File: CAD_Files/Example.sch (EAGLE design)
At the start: 9 parts, among them IC1 LM555D, Q1 BSS806N

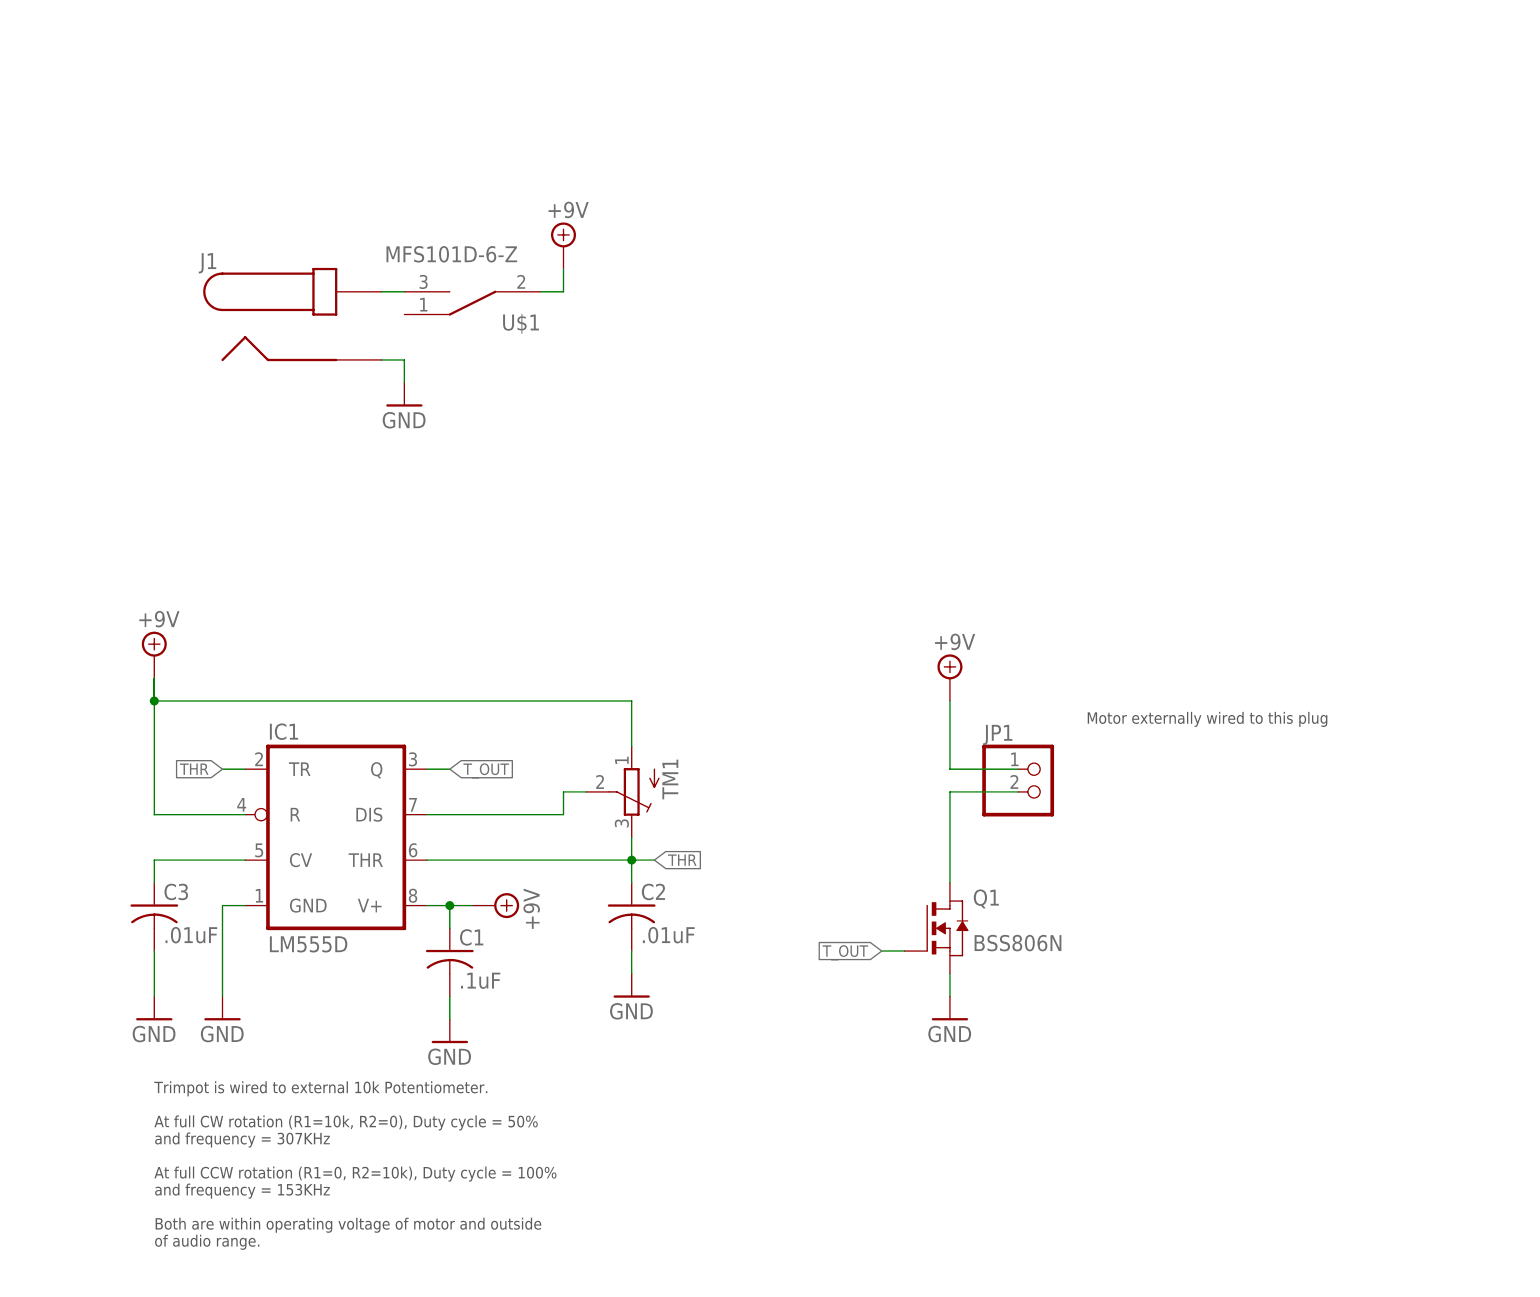
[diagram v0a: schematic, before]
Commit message: Added decoupling capacitors, fixed Library style guide compliance
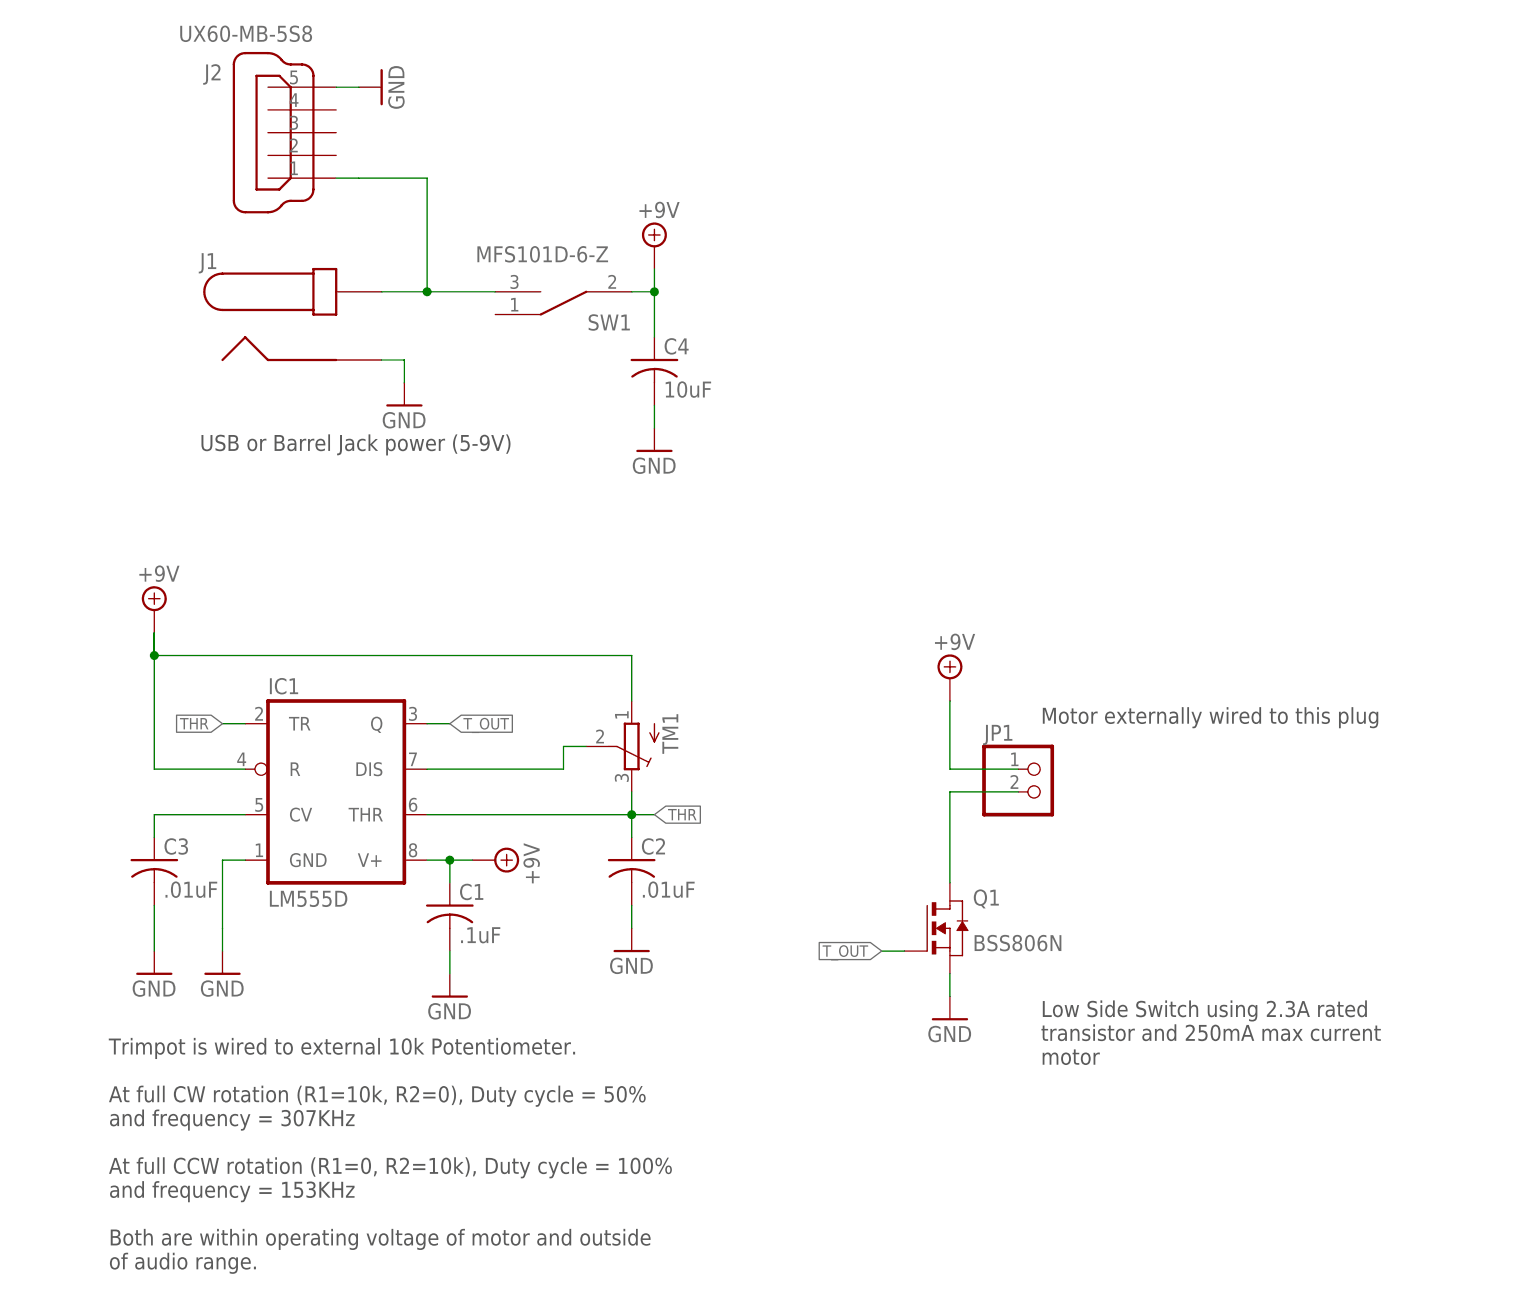
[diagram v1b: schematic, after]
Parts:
- removed U$1: MFS101D-6-Z, Example:MFS101D-6-Z
- added C4: 10uF, rcl:C-USC0603
- added J2: UX60-MB-5S8, RoboJackets-Connectors:UX60-MB-5S8
- added SW1: MFS101D-6-Z, Example:MFS101D-6-Z
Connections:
- removed net N$4: J1.1, U$1.B
- new net N$5: J1.1, J2.1, SW1.B
- net +9V: now also C4.1, SW1.COMMON; no longer U$1.COMMON
- net GND: now also C4.2, J2.5
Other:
- note added: "Low Side Switch using 2.3A rated transistor and 250mA max current motor"
- note added: "USB or Barrel Jack power (5-9V)"
- moved on the sheet: C1, C2, C3, IC1, TM1

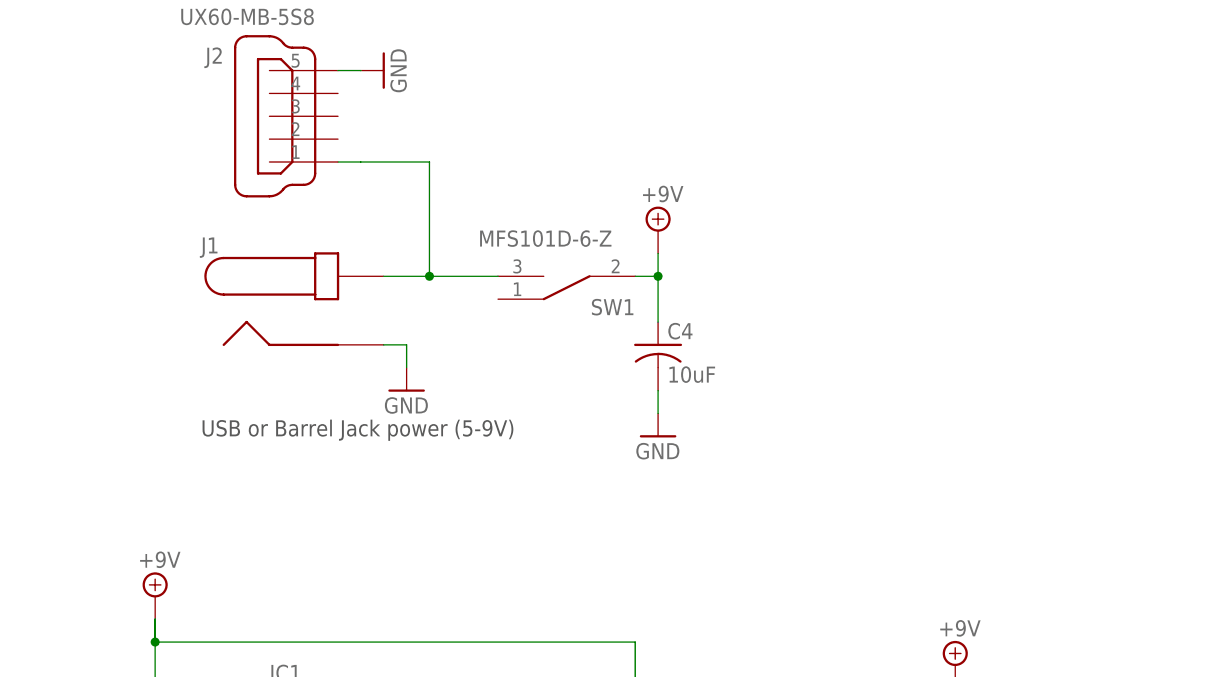
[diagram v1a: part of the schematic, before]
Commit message: Library edits, power switching transistor, 3d CAD
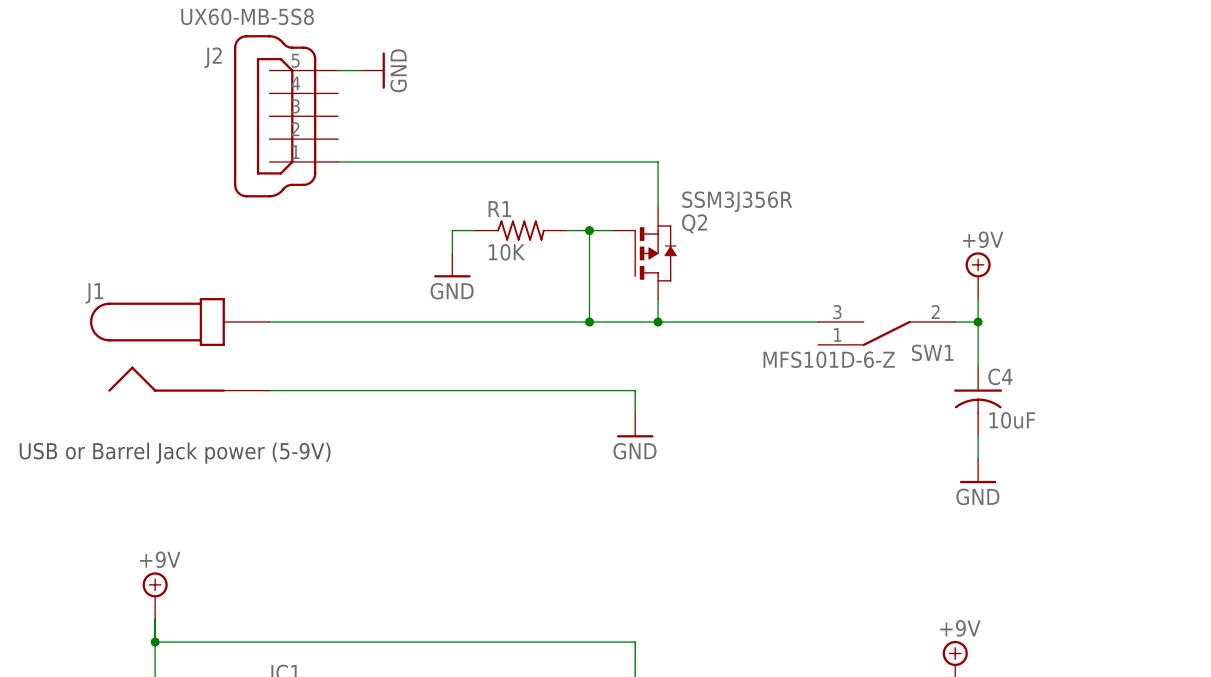
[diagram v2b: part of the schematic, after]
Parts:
- added Q2: SSM3J356R, Example:SSM3J356R
- added R1: 10K, rcl:R-US_R0603
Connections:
- removed net N$5: J1.1, J2.1, SW1.B
- new net N$4: J2.1, Q2.S
- new net N$6: J1.1, Q2.D, Q2.G, R1.2, SW1.B
- net GND: now also R1.1
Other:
- moved on the sheet: C4, J1, SW1
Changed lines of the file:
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@@
 <?xml version="1.0" encoding="utf-8"?>
 <!DOCTYPE eagle SYSTEM "eagle.dtd">
-<eagle version="9.5.2">
+<eagle version="9.6.2">
 <drawing>
 <settings>
@@
 <part name="SUPPLY12" library="RoboJackets-Supplies" deviceset="GND" device=""/>
 <part name="SW1" library="Example" deviceset="MFS101D-6-Z" device=""/>
+<part name="SUPPLY13" library="RoboJackets-Supplies" deviceset="GND" device=""/>
+<part name="R1" library="rcl" library_urn="urn:adsk.eagle:library:334" deviceset="R-US_" device="R0603" package3d_urn="urn:adsk.eagle:package:23555/3" value="10K"/>
+<part name="Q2" library="Example" deviceset="SSM3J356R" device="" package3d_urn="urn:adsk.eagle:package:24993154/1"/>
 </parts>
 <sheets>
@@
 transistor and 250mA max current
 motor</text>
-<text x="33.02" y="99.06" size="1.778" layer="97">USB or Barrel Jack power (5-9V)</text>
+<text x="12.7" y="96.52" size="1.778" layer="97">USB or Barrel Jack power (5-9V)</text>
 </plain>
 <instances>
@@
 <attribute name="VALUE" x="114.3" y="33.02" size="1.778" layer="96"/>
 </instance>
-<instance part="J1" gate="G$1" x="43.18" y="111.76" smashed="yes">
-<attribute name="NAME" x="33.02" y="119.38" size="1.778" layer="95"/>
-<attribute name="VALUE" x="33.02" y="106.68" size="1.778" layer="96"/>
+<instance part="J1" gate="G$1" x="30.48" y="106.68" smashed="yes">
+<attribute name="NAME" x="20.32" y="114.3" size="1.778" layer="95"/>
+<attribute name="VALUE" x="20.32" y="101.6" size="1.778" layer="96"/>
 </instance>
 <instance part="JP1" gate="G$1" x="127" y="60.96" smashed="yes">
@@
 <attribute name="VALUE" x="114.935" y="76.835" size="1.778" layer="96"/>
 </instance>
-<instance part="SUPPLY8" gate="G$1" x="55.88" y="104.14" smashed="yes">
-<attribute name="VALUE" x="53.34" y="101.6" size="1.778" layer="96"/>
-</instance>
-<instance part="SUPPLY9" gate="+9V" x="83.82" y="121.92" smashed="yes">
-<attribute name="VALUE" x="81.915" y="125.095" size="1.778" layer="96"/>
+<instance part="SUPPLY8" gate="G$1" x="81.28" y="99.06" smashed="yes">
+<attribute name="VALUE" x="78.74" y="96.52" size="1.778" layer="96"/>
+</instance>
+<instance part="SUPPLY9" gate="+9V" x="119.38" y="116.84" smashed="yes">
+<attribute name="VALUE" x="117.475" y="120.015" size="1.778" layer="96"/>
 </instance>
 <instance part="SUPPLY10" gate="G$1" x="27.94" y="40.64" smashed="yes">
@@
 <attribute name="VALUE" x="55.88" y="137.16" size="1.778" layer="96" rot="R90"/>
 </instance>
-<instance part="C4" gate="G$1" x="83.82" y="109.22" smashed="yes">
-<attribute name="NAME" x="84.836" y="109.855" size="1.778" layer="95"/>
-<attribute name="VALUE" x="84.836" y="105.029" size="1.778" layer="96"/>
-</instance>
-<instance part="SUPPLY12" gate="G$1" x="83.82" y="99.06" smashed="yes">
-<attribute name="VALUE" x="81.28" y="96.52" size="1.778" layer="96"/>
-</instance>
-<instance part="SW1" gate="G$1" x="73.66" y="116.84" smashed="yes" rot="R180">
-<attribute name="NAME" x="81.28" y="114.3" size="1.778" layer="95" rot="R180"/>
-<attribute name="VALUE" x="78.74" y="121.92" size="1.778" layer="96" rot="R180"/>
+<instance part="C4" gate="G$1" x="119.38" y="104.14" smashed="yes">
+<attribute name="NAME" x="120.396" y="104.775" size="1.778" layer="95"/>
+<attribute name="VALUE" x="120.396" y="99.949" size="1.778" layer="96"/>
+</instance>
+<instance part="SUPPLY12" gate="G$1" x="119.38" y="93.98" smashed="yes">
+<attribute name="VALUE" x="116.84" y="91.44" size="1.778" layer="96"/>
+</instance>
+<instance part="SW1" gate="G$1" x="109.22" y="111.76" smashed="yes" rot="R180">
+<attribute name="NAME" x="116.84" y="109.22" size="1.778" layer="95" rot="R180"/>
+<attribute name="VALUE" x="110.236" y="108.458" size="1.778" layer="96" rot="R180"/>
+</instance>
+<instance part="SUPPLY13" gate="G$1" x="60.96" y="116.84" smashed="yes">
+<attribute name="VALUE" x="58.42" y="114.3" size="1.778" layer="96"/>
+</instance>
+<instance part="R1" gate="G$1" x="68.58" y="121.92" smashed="yes">
+<attribute name="NAME" x="64.77" y="123.4186" size="1.778" layer="95"/>
+<attribute name="VALUE" x="64.77" y="118.618" size="1.778" layer="96"/>
+</instance>
+<instance part="Q2" gate="G$1" x="83.82" y="119.38" smashed="yes">
+<attribute name="VALUE" x="86.36" y="124.46" size="1.778" layer="96"/>
+<attribute name="NAME" x="86.36" y="121.92" size="1.778" layer="95"/>
 </instance>
 </instances>
@@
 <segment>
 <pinref part="J1" gate="G$1" pin="2"/>
-<wire x1="53.34" y1="109.22" x2="55.88" y2="109.22" width="0.1524" layer="91"/>
+<wire x1="40.64" y1="104.14" x2="81.28" y2="104.14" width="0.1524" layer="91"/>
 <pinref part="SUPPLY8" gate="G$1" pin="GND"/>
-<wire x1="55.88" y1="109.22" x2="55.88" y2="106.68" width="0.1524" layer="91"/>
+<wire x1="81.28" y1="104.14" x2="81.28" y2="101.6" width="0.1524" layer="91"/>
 </segment>
 <segment>
@@
 <pinref part="SUPPLY12" gate="G$1" pin="GND"/>
 <pinref part="C4" gate="G$1" pin="2"/>
-<wire x1="83.82" y1="101.6" x2="83.82" y2="104.14" width="0.1524" layer="91"/>
+<wire x1="119.38" y1="96.52" x2="119.38" y2="99.06" width="0.1524" layer="91"/>
+</segment>
+<segment>
+<pinref part="SUPPLY13" gate="G$1" pin="GND"/>
+<wire x1="60.96" y1="119.38" x2="60.96" y2="121.92" width="0.1524" layer="91"/>
+<pinref part="R1" gate="G$1" pin="1"/>
+<wire x1="60.96" y1="121.92" x2="63.5" y2="121.92" width="0.1524" layer="91"/>
 </segment>
 </net>
@@
 <segment>
 <pinref part="SUPPLY9" gate="+9V" pin="+9V"/>
-<wire x1="83.82" y1="116.84" x2="83.82" y2="119.38" width="0.1524" layer="91"/>
-<wire x1="81.28" y1="116.84" x2="83.82" y2="116.84" width="0.1524" layer="91"/>
+<wire x1="119.38" y1="111.76" x2="119.38" y2="114.3" width="0.1524" layer="91"/>
+<wire x1="116.84" y1="111.76" x2="119.38" y2="111.76" width="0.1524" layer="91"/>
 <pinref part="C4" gate="G$1" pin="1"/>
-<wire x1="83.82" y1="111.76" x2="83.82" y2="116.84" width="0.1524" layer="91"/>
-<junction x="83.82" y="116.84"/>
+<wire x1="119.38" y1="106.68" x2="119.38" y2="111.76" width="0.1524" layer="91"/>
+<junction x="119.38" y="111.76"/>
 <pinref part="SW1" gate="G$1" pin="COMMON"/>
 </segment>
@@
 </segment>
 </net>
-<net name="N$5" class="0">
+<net name="N$4" class="0">
 <segment>
 <pinref part="J2" gate="G$1" pin="1"/>
-<wire x1="48.26" y1="129.54" x2="50.8" y2="129.54" width="0.1524" layer="91"/>
-<wire x1="50.8" y1="129.54" x2="58.42" y2="129.54" width="0.1524" layer="91"/>
+<wire x1="48.26" y1="129.54" x2="83.82" y2="129.54" width="0.1524" layer="91"/>
+<wire x1="83.82" y1="129.54" x2="83.82" y2="124.46" width="0.1524" layer="91"/>
+<pinref part="Q2" gate="G$1" pin="S"/>
+</segment>
+</net>
+<net name="N$6" class="0">
+<segment>
+<pinref part="R1" gate="G$1" pin="2"/>
+<wire x1="78.74" y1="121.92" x2="76.2" y2="121.92" width="0.1524" layer="91"/>
+<pinref part="Q2" gate="G$1" pin="G"/>
 <pinref part="J1" gate="G$1" pin="1"/>
-<wire x1="53.34" y1="116.84" x2="58.42" y2="116.84" width="0.1524" layer="91"/>
-<wire x1="58.42" y1="116.84" x2="66.04" y2="116.84" width="0.1524" layer="91"/>
-<wire x1="58.42" y1="129.54" x2="58.42" y2="116.84" width="0.1524" layer="91"/>
-<junction x="58.42" y="116.84"/>
+<wire x1="76.2" y1="121.92" x2="73.66" y2="121.92" width="0.1524" layer="91"/>
+<wire x1="40.64" y1="111.76" x2="76.2" y2="111.76" width="0.1524" layer="91"/>
 <pinref part="SW1" gate="G$1" pin="B"/>
-</segment>
-</net>
+<wire x1="76.2" y1="111.76" x2="83.82" y2="111.76" width="0.1524" layer="91"/>
+<wire x1="83.82" y1="111.76" x2="101.6" y2="111.76" width="0.1524" layer="91"/>
+<wire x1="83.82" y1="114.3" x2="83.82" y2="111.76" width="0.1524" layer="91"/>
+<junction x="83.82" y="111.76"/>
+<pinref part="Q2" gate="G$1" pin="D"/>
+<wire x1="76.2" y1="121.92" x2="76.2" y2="111.76" width="0.1524" layer="91"/>
+<junction x="76.2" y="121.92"/>
+<junction x="76.2" y="111.76"/>
+</segment>
+</net>
